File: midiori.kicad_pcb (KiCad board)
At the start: 2 copper layers, 141 x 150 mm, 45 parts, among them J1 x68000_expansion, J2 Conn_ARM_JTAG_SWD_10, J4 Mini-DIN-5, U1 74LCX07, U10 ICE40HX1K-VQ100, U11 TLV73333PDBV, U2 AT25SF081-SSHD-X, U3 TLV73312PDBV, U4 SN74LVC8T245DWR, U5 SN74LVC8T245DWR, U6 SN74LVC8T245DWR, U7 SN74LVC8T245DWR, U8 SN74LVC8T245DWR, U9 SN74LVC8T245DWR, X1 16MHz

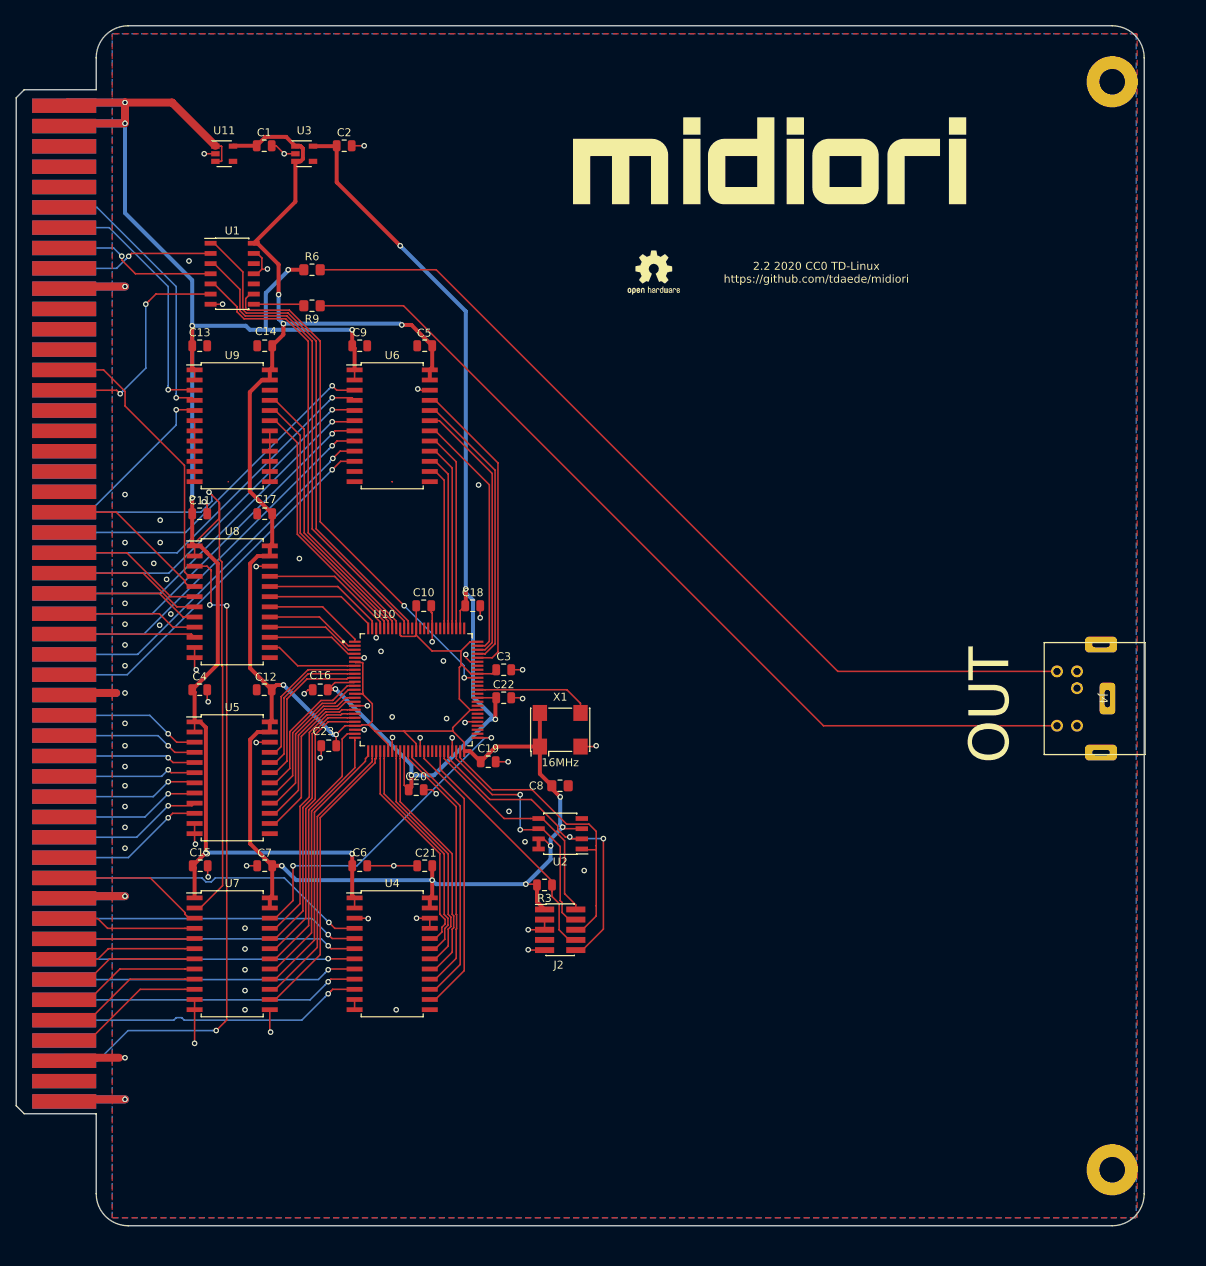
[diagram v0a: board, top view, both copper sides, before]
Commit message: Added synth addon
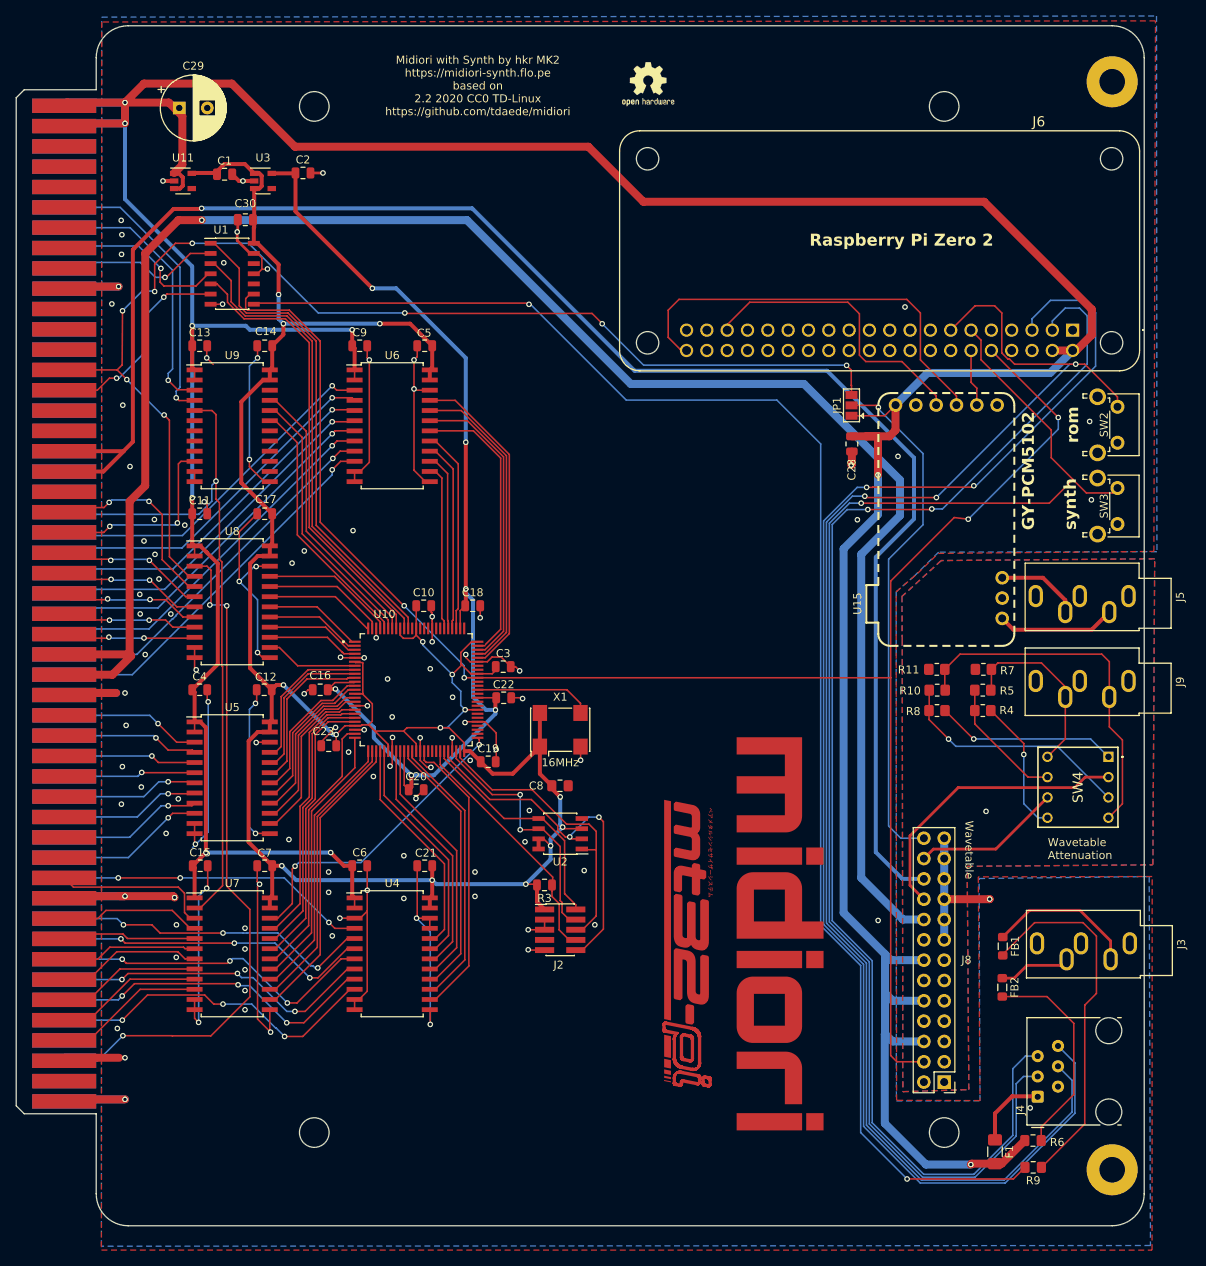
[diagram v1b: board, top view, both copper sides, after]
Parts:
- added C28: 0.1uF, Capacitor_SMD:C_0805_2012Metric, F.Cu at (148.5, 91.3)
- added C29: 220uF, Capacitor_THT:CP_Radial_D8.0mm_P3.50mm, F.Cu at (64.4, 49.3)
- added C30: 0.1uF, Capacitor_SMD:C_0805_2012Metric, F.Cu at (72.6, 63.2)
- added F1: 500mA hold, 1A trip, Fuse:Fuse_1206_3216Metric_Pad1.42x1.75mm_HandSolder, F.Cu at (166.3, 179.8)
- added FB1: 100kOhms @ 100 MHz, Inductor_SMD:L_0805_2012Metric_Pad1.05x1.20mm_HandSolder, F.Cu at (167.3, 154.1)
- added FB2: 100kOhms @ 100 MHz, Inductor_SMD:L_0805_2012Metric_Pad1.05x1.20mm_HandSolder, F.Cu at (167.3, 159.2)
- added J3: AudioJack3, Connector_Audio:Jack_3.5mm_CUI_SJ1-3535NG_Horizontal, F.Cu at (183.2, 153.7)
- added J5: AudioJack3, Connector_Audio:Jack_3.5mm_CUI_SJ1-3535NG_Horizontal, F.Cu at (183.0, 110.3)
- added J6: J_PI_ZERO, pizero:RASPBERRYPIZEROWV13, F.Cu at (152.2, 67.1)
- added J8: Waveblaster Connector, Connector_PinHeader_2.54mm:PinHeader_2x13_P2.54mm_Vertical, F.Cu at (160.0, 171.0)
- added J9: AudioJack3, Connector_Audio:Jack_3.5mm_CUI_SJ1-3535NG_Horizontal, F.Cu at (183.0, 120.9)
- added JP1: SolderJumper_3_Open, Jumper:SolderJumper-3_P1.3mm_Open_Pad1.0x1.5mm, F.Cu at (148.4, 86.5)
- added R10: 47k, Resistor_SMD:R_0805_2012Metric_Pad1.20x1.40mm_HandSolder, F.Cu at (159.1, 122.0)
- added R11: 47k, Resistor_SMD:R_0805_2012Metric_Pad1.20x1.40mm_HandSolder, F.Cu at (159.1, 119.5)
- added R4: 47k, Resistor_SMD:R_0805_2012Metric_Pad1.20x1.40mm_HandSolder, F.Cu at (164.8, 124.6)
- added R5: 47k, Resistor_SMD:R_0805_2012Metric_Pad1.20x1.40mm_HandSolder, F.Cu at (164.8, 122.0)
- added R7: 47k, Resistor_SMD:R_0805_2012Metric_Pad1.20x1.40mm_HandSolder, F.Cu at (164.9, 119.5)
- added R8: 47k, Resistor_SMD:R_0805_2012Metric_Pad1.20x1.40mm_HandSolder, F.Cu at (159.1, 124.6)
- added REF**: mt32pi, mt32pi-logo:mt32pi, F.Cu at (130.5, 156.8)
- added REF**: MountingHole_3.7mm, MountingHole:MountingHole_3.7mm, F.Cu at (160.0, 49.1)
- added REF**: MountingHole_3.7mm, MountingHole:MountingHole_3.7mm, F.Cu at (81.3, 49.1)
- added REF**: MountingHole_3.7mm, MountingHole:MountingHole_3.7mm, F.Cu at (160.0, 177.3)
- added REF**: MountingHole_3.7mm, MountingHole:MountingHole_3.7mm, F.Cu at (81.3, 177.3)
- added SW2: ROM, Button_Switch_THT:SW_Tactile_SPST_Angled_PTS645Vx58-2LFS, F.Cu at (181.7, 86.6)
- added SW3: SYNTH, Button_Switch_THT:SW_Tactile_SPST_Angled_PTS645Vx58-2LFS, F.Cu at (181.7, 96.8)
- added SW4: SS-10-23NPE, SS-10-23NPE:SS1023NPE, F.Cu at (180.5, 130.4)
- added U15: U_GY-PCM5102, llama:U_GY-PCM5102, F.Cu at (160.3, 100.7)
- J4: value Mini-DIN-5 -> RJ12; footprint x68k:MD-50SM -> Connector_RJ:RJ12_Amphenol_54601-x06_Horizontal
- U11: value TLV73333PDBV -> TLV75533PDBV
- moved R6 141.3 mm to (171.1, 178.3)
- moved R9 140.5 mm to (171.1, 181.7)
- moved svg2mod 98.1 mm to (139.5, 154.0), turned to -90 degrees
- moved J4 50.5 mm to (171.7, 172.9), turned to 90 degrees
- moved REF** 23.6 mm to (123.0, 46.3)
- moved C2 6.17 mm to (79.8, 57.4)
- moved U11 6.17 mm to (64.8, 58.4)
- moved U3 6.17 mm to (74.8, 58.4)
- moved C1 6.10 mm to (70.0, 57.6)
- moved C3 0.39 mm to (104.9, 119.1)
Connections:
- net Net-(J1-PadA13) renamed /DB8
- net Net-(J1-PadA14) renamed /DB9
- net Net-(J1-PadA15) renamed /DB10
- net Net-(J1-PadA16) renamed /DB11
- net Net-(J1-PadA17) renamed /DB12
- net Net-(J1-PadA18) renamed /DB13
- net Net-(J1-PadA19) renamed /DB14
- net Net-(J1-PadA20) renamed /DB15
- net Net-(R9-Pad2) renamed /midi_out
- net Net-(U1-Pad9) renamed /midi_UART_TX
- net Net-(U10-Pad65) renamed /sw2
- J1 pad A2: Net-(J1-PadA2) -> unconnected-(J1-PadA2)
- J1 pad A22: Net-(J1-PadA22) -> /+12V
- J1 pad A23: Net-(J1-PadA23) -> /+12V
- J1 pad A29: Net-(J1-PadA29) -> /UDS
- J1 pad A31: Net-(J1-PadA31) -> unconnected-(J1-PadA31)
- J1 pad A32: Net-(J1-PadA32) -> /-12V
- J1 pad A33: Net-(J1-PadA33) -> /-12V
- J1 pad A34: Net-(J1-PadA34) -> unconnected-(J1-PadA34)
- J1 pad A35: Net-(J1-PadA35) -> unconnected-(J1-PadA35)
- J1 pad A38: Net-(J1-PadA38) -> unconnected-(J1-PadA38)
- J1 pad A39: Net-(J1-PadA39) -> unconnected-(J1-PadA39)
- J1 pad A40: Net-(J1-PadA40) -> unconnected-(J1-PadA40)
- J1 pad A42: Net-(J1-PadA42) -> unconnected-(J1-PadA42)
- J1 pad A43: Net-(J1-PadA43) -> unconnected-(J1-PadA43)
- J1 pad A44: Net-(J1-PadA44) -> unconnected-(J1-PadA44)
- J1 pad A45: Net-(J1-PadA45) -> unconnected-(J1-PadA45)
- J1 pad A46: Net-(J1-PadA46) -> unconnected-(J1-PadA46)
- J1 pad A47: Net-(J1-PadA47) -> unconnected-(J1-PadA47)
- J1 pad A48: Net-(J1-PadA48) -> unconnected-(J1-PadA48)
- J1 pad B2: Net-(J1-PadB2) -> unconnected-(J1-PadB2)
- J1 pad B31: Net-(J1-PadB31) -> unconnected-(J1-PadB31)
- J1 pad B32: Net-(J1-PadB32) -> unconnected-(J1-PadB32)
- J1 pad B33: Net-(J1-PadB33) -> unconnected-(J1-PadB33)
- J1 pad B34: Net-(J1-PadB34) -> unconnected-(J1-PadB34)
- J1 pad B35: Net-(J1-PadB35) -> unconnected-(J1-PadB35)
- J1 pad B36: Net-(J1-PadB36) -> unconnected-(J1-PadB36)
- J1 pad B37: Net-(J1-PadB37) -> unconnected-(J1-PadB37)
- J1 pad B38: Net-(J1-PadB38) -> unconnected-(J1-PadB38)
- J1 pad B39: Net-(J1-PadB39) -> unconnected-(J1-PadB39)
- J1 pad B4: Net-(J1-PadB4) -> unconnected-(J1-PadB4)
- J1 pad B40: Net-(J1-PadB40) -> unconnected-(J1-PadB40)
- J1 pad B46: Net-(J1-PadB46) -> unconnected-(J1-PadB46)
- J1 pad B47: Net-(J1-PadB47) -> unconnected-(J1-PadB47)
- J1 pad B48: Net-(J1-PadB48) -> unconnected-(J1-PadB48)
- J2 pad 7: Net-(J2-Pad7) -> unconnected-(J2-KEY-Pad7)
- J4 pad 3: Net-(J4-Pad3) -> /synth_sw
- J4 pad 4: Net-(J4-Pad4) -> /rom_sw
- J4 pad 5: Net-(J4-Pad5) -> /PI_SDA
- R6 pad 2: Net-(J4-Pad4) -> Net-(FB2-Pad2)
- R9 pad 1: Net-(J4-Pad5) -> Net-(FB1-Pad2)
- U1 pad 10: Net-(U1-Pad10) -> unconnected-(U1-Pad10)
- U1 pad 12: Net-(U1-Pad12) -> unconnected-(U1-Pad12)
- U10 pad 41: Net-(U10-Pad41) -> unconnected-(U10-IOB_42_CBSEL0-Pad41)
- U10 pad 42: Net-(U10-Pad42) -> unconnected-(U10-IOB_43_CBSEL1-Pad42)
- U10 pad 43: Net-(U10-Pad43) -> unconnected-(U10-CDONE-Pad43)
- U10 pad 52: Net-(U10-Pad52) -> unconnected-(U10-IOR_53-Pad52)
- U10 pad 53: Net-(U10-Pad53) -> unconnected-(U10-IOR_54-Pad53)
- U10 pad 54: Net-(U10-Pad54) -> unconnected-(U10-IOR_55-Pad54)
- U10 pad 56: Net-(U10-Pad56) -> unconnected-(U10-IOR_56-Pad56)
- U10 pad 57: Net-(U10-Pad57) -> unconnected-(U10-IOR_57-Pad57)
- U10 pad 59: Net-(U10-Pad59) -> unconnected-(U10-IOR_58-Pad59)
- U10 pad 60: Net-(U10-Pad60) -> unconnected-(U10-IOR_59-Pad60)
- U10 pad 62: Net-(U10-Pad62) -> unconnected-(U10-IOR_60_GBIN3-Pad62)
- U10 pad 64: Net-(U10-Pad64) -> unconnected-(U10-IOR_63-Pad64)
- U10 pad 68: Net-(U10-Pad68) -> unconnected-(U10-IOR_67-Pad68)
- U10 pad 69: Net-(U10-Pad69) -> unconnected-(U10-IOR_68-Pad69)
- U10 pad 76: Net-(U10-Pad76) -> unconnected-(U10-VPP_FAST-Pad76)
- U10 pad 82: Net-(U10-Pad82) -> unconnected-(U10-IOT_78-Pad82)
- U10 pad 83: Net-(U10-Pad83) -> unconnected-(U10-IOT_79-Pad83)
- U10 pad 85: Net-(U10-Pad85) -> unconnected-(U10-IOT_80-Pad85)
- U10 pad 86: Net-(U10-Pad86) -> unconnected-(U10-IOT_81-Pad86)
- U10 pad 87: Net-(U10-Pad87) -> unconnected-(U10-IOT_82-Pad87)
- U10 pad 89: Net-(U10-Pad89) -> unconnected-(U10-IOT_84_GBIN1-Pad89)
- U11 pad 4: Net-(U11-Pad4) -> unconnected-(U11-NC-Pad4)
- U3 pad 4: Net-(U3-Pad4) -> unconnected-(U3-NC-Pad4)
- U9 pad 10: GND -> /UDS
- U9 pad 14: GND -> /uds
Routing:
- net +5V: track 227.3 -> 527.6 mm, vias 8 -> 9
- net /+12V: track 0.00 -> 240.0 mm, vias 0 -> 1
- net GND: track 166.7 -> 397.8 mm, vias 81 -> 121
- net /-12V: track 0.00 -> 212.9 mm, vias 0 -> 1
- net /rom_sw: track 0.00 -> 186.6 mm, vias 0 -> 3
- net /midi_out: track 6.33 -> 189.9 mm, vias 0 -> 2
- net /PI_SCL: track 0.00 -> 179.6 mm, vias 0 -> 2
- net /synth_sw: track 0.00 -> 173.2 mm, vias 0 -> 1
- net /PI_SDA: track 0.00 -> 164.0 mm, vias 0 -> 2
- net /midi_UART_TX: track 64.7 -> 222.4 mm, vias 2 -> 4
- net /EXRESET: track 35.9 -> 151.0 mm, vias 0 -> 8
- net Net-(J4-Pad5): track 113.8 -> 0.00 mm
- net Net-(J4-Pad4): track 112.9 -> 0.00 mm
- net /WT_RESET: track 0.00 -> 64.9 mm, vias 0 -> 1
- net /I2S_DIN: track 0.00 -> 52.5 mm
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- added copper zone on B.Cu, net /AGND
- added copper zone on F.Cu, net /AGND
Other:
- net class Default removed
- board text added: "GY-PCM5102"
- board text added: "Midiori with Synth by hkr MK2 https://midiori-synth.flo.pe based on 2.2 2020 CC0 TD-Linux https://github.com/tdaede/midiori"
- board text added: "Raspberry Pi Zero 2"
- board text added: "Wavetable"
- board text added: "Wavetable Attenuation"
- board text added: "rom"
- board text added: "synth"
- board text removed: "2.2 2020 CC0 TD-Linux https://github.com/tdaede/midiori"
- board text removed: "OUT"

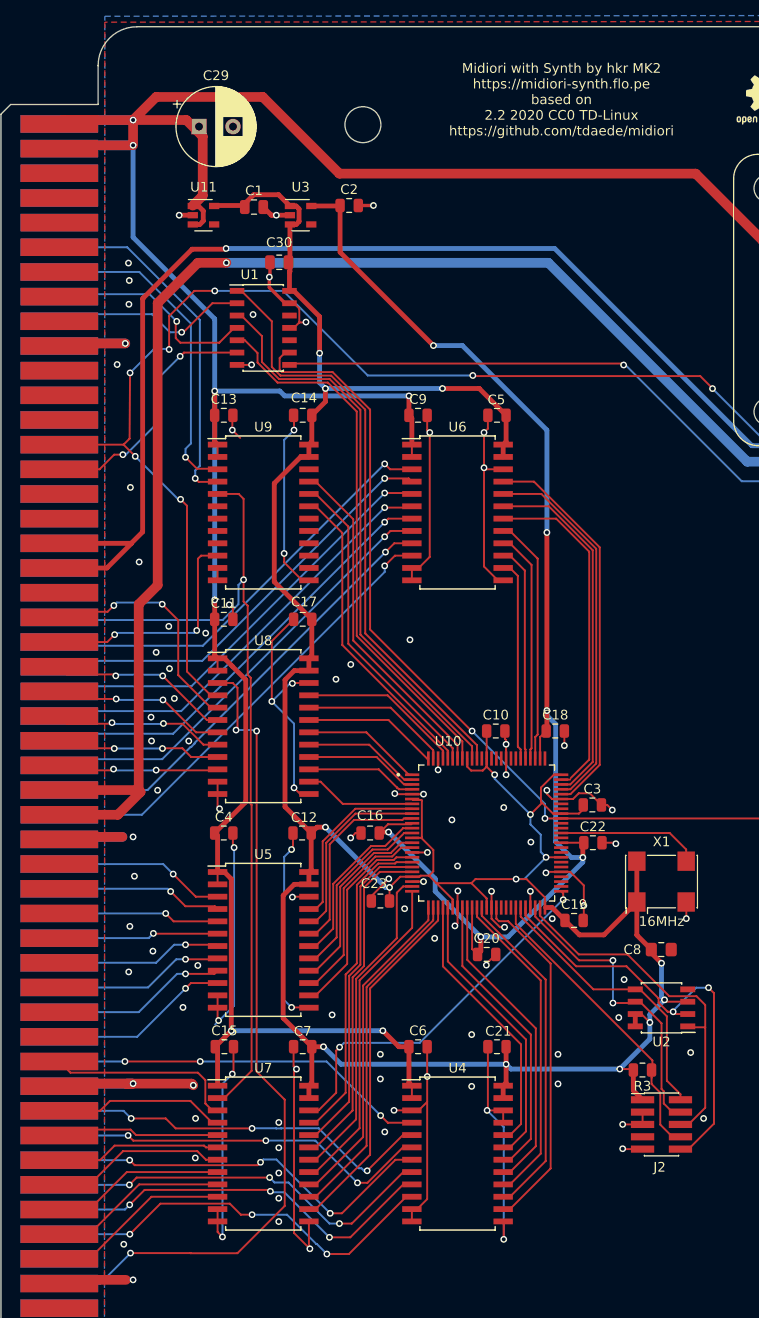
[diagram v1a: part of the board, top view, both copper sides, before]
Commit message: Fixed some traces
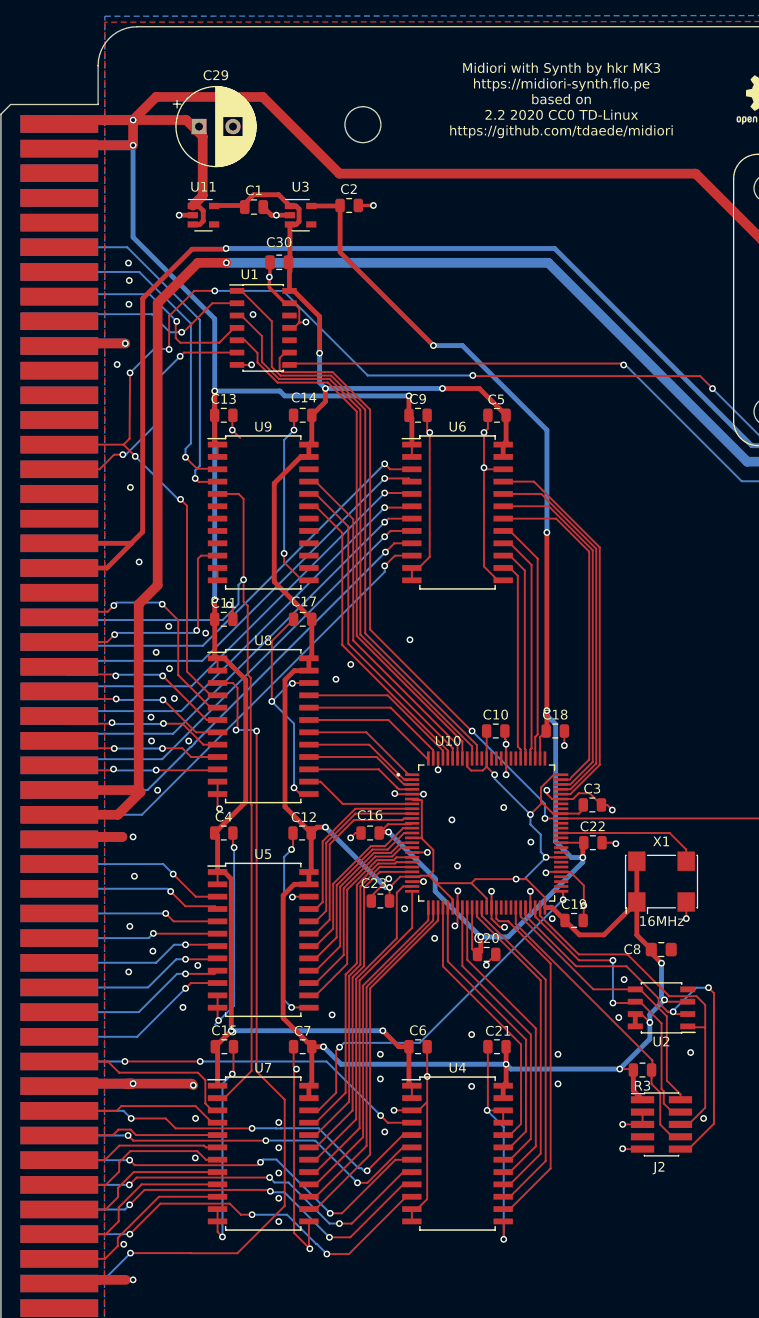
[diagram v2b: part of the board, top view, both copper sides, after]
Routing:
- net /DB1: track 18.4 -> 19.3 mm
- net /DB2: track 17.9 -> 18.5 mm
- net /DB3: track 18.1 -> 18.7 mm
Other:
- board text added: "Midiori with Synth by hkr MK3 https://midiori-synth.flo.pe based on 2.2 2020 CC0 TD-Linux https://github.com/tdaede/midiori"
- board text removed: "Midiori with Synth by hkr MK2 https://midiori-synth.flo.pe based on 2.2 2020 CC0 TD-Linux https://github.com/tdaede/midiori"

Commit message: Development board
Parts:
- removed SW4: SS-10-23NPE, SS-10-23NPE:SS1023NPE
- removed U15: U_GY-PCM5102, llama:U_GY-PCM5102
- added C24: 0.1uF, Capacitor_SMD:C_0805_2012Metric, F.Cu at (82.0, 77.0)
- added C25: 47uF, Capacitor_SMD:C_Elec_6.3x5.8, F.Cu at (123.3, 93.3)
- added C26: 47uF, Capacitor_SMD:C_Elec_6.3x5.8, F.Cu at (132.9, 93.3)
- added C27: 5.6nF, Capacitor_SMD:C_0805_2012Metric, F.Cu at (137.6, 107.4)
- added C31: 10nF, Capacitor_SMD:C_0805_2012Metric, F.Cu at (96.5, 66.9)
- added C32: 10nF, Capacitor_SMD:C_0805_2012Metric, F.Cu at (96.5, 64.0)
- added C33: 47uF, Capacitor_SMD:C_Elec_6.3x5.8, B.Cu at (126.1, 93.1)
- added C34: 47uF, Capacitor_SMD:C_Elec_6.3x5.8, B.Cu at (116.3, 93.1)
- added C35: 5.6nF, Capacitor_SMD:C_0805_2012Metric, B.Cu at (136.9, 92.7)
- added C36: 5.6nF, Capacitor_SMD:C_0805_2012Metric, B.Cu at (134.9, 92.7)
- added J10: AudioJack3, Connector_Audio:Jack_3.5mm_CUI_SJ1-3535NG_Horizontal, F.Cu at (183.1, 131.4)
- added J11: PCM1802_board, Audio_Module:PCM1808_board, B.Cu at (91.2, 93.1)
- added J12: Conn_01x03_Pin, Connector_PinHeader_2.54mm:PinHeader_1x03_P2.54mm_Horizontal, B.Cu at (133.9, 98.2)
- added J7: AMP2, Audio_Module:AMP2_TH, F.Cu at (93.0, 79.2)
- added JP2: Jumper_3_Open, Jumper:SolderJumper-3_P1.3mm_Open_RoundedPad1.0x1.5mm, F.Cu at (98.2, 85.8)
- added JP3: Jumper_3_Open, Jumper:SolderJumper-3_P1.3mm_Open_RoundedPad1.0x1.5mm, F.Cu at (95.1, 85.8)
- added JP4: Jumper_3_Open, Jumper:SolderJumper-3_P1.3mm_Open_RoundedPad1.0x1.5mm, F.Cu at (92.1, 85.8)
- added R1: 18k, Resistor_SMD:R_0805_2012Metric, F.Cu at (110.8, 100.3)
- added R12: 560, Resistor_SMD:R_0805_2012Metric, B.Cu at (138.9, 92.7)
- added R13: 560, Resistor_SMD:R_0805_2012Metric, B.Cu at (132.9, 92.7)
- added R2: 18k, Resistor_SMD:R_0805_2012Metric, F.Cu at (111.0, 97.6)
- added SW1: RotaryEncoder_Switch, Rotary_Encoder:RotaryEncoder_Bourns_Horizontal_PEC09-2xxxF-Sxxxx, F.Cu at (179.9, 145.3)
- added X2: 12.288MHz, Oscillator:Oscillator_SMD_SeikoEpson_SG8002CA-4Pin_7.0x5.0mm, F.Cu at (87.7, 78.4)
- C28: value 0.1uF -> 5.6nF
- R10, R11, R7, R8: value 47k -> 10k; footprint Resistor_SMD:R_0805_2012Metric_Pad1.20x1.40mm_HandSolder -> Resistor_SMD:R_0805_2012Metric
- R4, R5: value 47k -> 560; footprint Resistor_SMD:R_0805_2012Metric_Pad1.20x1.40mm_HandSolder -> Resistor_SMD:R_0805_2012Metric
- moved R8 90.8 mm to (89.0, 66.8), turned to 0 degrees
- moved R11 89.4 mm to (88.9, 64.1)
- moved R7 89.2 mm to (92.8, 66.9), turned to 180 degrees
- moved R10 88.2 mm to (92.7, 64.0)
- moved C9 54.6 mm to (125.3, 117.9), turned to 180 degrees
- moved REF** 47.2 mm to (170.2, 45.7)
- moved C5 44.4 mm to (115.8, 118.2)
- moved U6 35.8 mm to (121.5, 107.6), turned to 180 degrees
- moved R4 34.8 mm to (136.6, 104.2), turned to -90 degrees
- moved R5 30.5 mm to (140.1, 104.2), turned to -90 degrees
- moved C28 16.3 mm to (142.3, 106.4), turned to -90 degrees
- moved C2 5.03 mm to (75.9, 54.3), turned to 90 degrees
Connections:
- C28 pad 1: GND -> /RIGHT_OUT
- C28 pad 2: +5V -> AGND
- J5 pad R: /RIGHT -> /RIGHT_OUT
- J5 pad S: /AGND -> AGND
- J5 pad T: /LEFT -> /LEFT_OUT
- J6 pad 12: /I2S_BCK -> /bclk
- J6 pad 35: /I2S_LCK -> /lrclk
- J6 pad 40: /I2S_DIN -> /sdata_pi
- J8 pad 1: /AGND -> AGND
- J8 pad 11: /AGND -> AGND
- J8 pad 3: /AGND -> AGND
- J8 pad 5: /AGND -> AGND
- J8 pad 7: /AGND -> AGND
- J8 pad 9: /AGND -> AGND
- J9 pad R: /R_Hi -> /ADC0_R
- J9 pad S: /AGND -> AGND
- J9 pad T: /L_Hi -> /ADC0_L
- R10 pad 1: /L_Med -> Net-(R10-Pad1)
- R10 pad 2: /L_Hi -> /rot_b
- R11 pad 1: /AGND -> +3V3
- R11 pad 2: /L_Hi -> Net-(R10-Pad1)
- R4 pad 1: /R_Lo -> Net-(C25-Pad2)
- R4 pad 2: /R_Med -> /LEFT_OUT
- R5 pad 1: /R_Med -> Net-(C26-Pad2)
- R5 pad 2: /R_Hi -> /RIGHT_OUT
- R7 pad 1: /AGND -> /rot_a
- R7 pad 2: /R_Hi -> Net-(R7-Pad2)
- R8 pad 1: /L_Lo -> +3V3
- R8 pad 2: /L_Med -> Net-(R7-Pad2)
- U10 pad 82: unconnected-(U10-IOT_78-Pad82) -> /mix_pwm
- U10 pad 83: unconnected-(U10-IOT_79-Pad83) -> /mix_d0
- U10 pad 86: unconnected-(U10-IOT_81-Pad86) -> /mix_d1
- U10 pad 89: unconnected-(U10-IOT_84_GBIN1-Pad89) -> /mix_d2
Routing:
- net AGND: track 0.00 -> 301.6 mm, vias 0 -> 6
- net /rot_sw: track 0.00 -> 235.7 mm, vias 0 -> 1
- net Net-(R10-Pad1): track 0.00 -> 234.3 mm, vias 0 -> 1
- net Net-(R7-Pad2): track 0.00 -> 225.9 mm, vias 0 -> 1
- net /WT_L: track 18.6 -> 146.2 mm, vias 0 -> 1
- net /WT_R: track 36.5 -> 138.5 mm, vias 0 -> 1
- net /bclk: track 0.00 -> 86.3 mm
- net /ADC0_L: track 0.00 -> 85.2 mm
- net /ADC0_R: track 0.00 -> 79.6 mm
- net +3V3: track 307.2 -> 365.5 mm, vias 15 -> 19
- net GND: track 397.8 -> 340.4 mm, vias 121 -> 126
- net /lrclk: track 0.00 -> 54.6 mm, vias 0 -> 1
- net /I2S_DIN: track 52.5 -> 0.00 mm
- net /LEFT_OUT: track 0.00 -> 50.8 mm
- net /L_Hi: track 45.3 -> 0.00 mm
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- added copper zone on B.Cu, net AGND
- added copper zone on F.Cu, net AGND
- removed copper zone on B.Cu, net /AGND
- removed copper zone on F.Cu, net /AGND
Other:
- board text added: "FMT"
- board text added: "GND"
- board text added: "L"
- board text added: "MD0"
- board text added: "MD1"
- board text added: "Midiori with Synth and Mixer by hkr prototype 1 based on 2.2 2020 CC0 TD-Linux https://github.com/tdaede/midiori"
- board text added: "R"
- board text removed: "GY-PCM5102"
- board text removed: "Midiori with Synth by hkr MK3 https://midiori-synth.flo.pe based on 2.2 2020 CC0 TD-Linux https://github.com/tdaede/midiori"
- board text removed: "Wavetable Attenuation"
